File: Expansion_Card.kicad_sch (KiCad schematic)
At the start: 38 parts, among them J1 Conn_01x03_MountingPin, J2 Conn_01x03_MountingPin, P1 USB_C_Plug_USB2.0, SW1 SW_Push, SW2 SW_Push, U1 AP2112K-3.3, U2 RP2354A, Y1 ABM8-272-T3

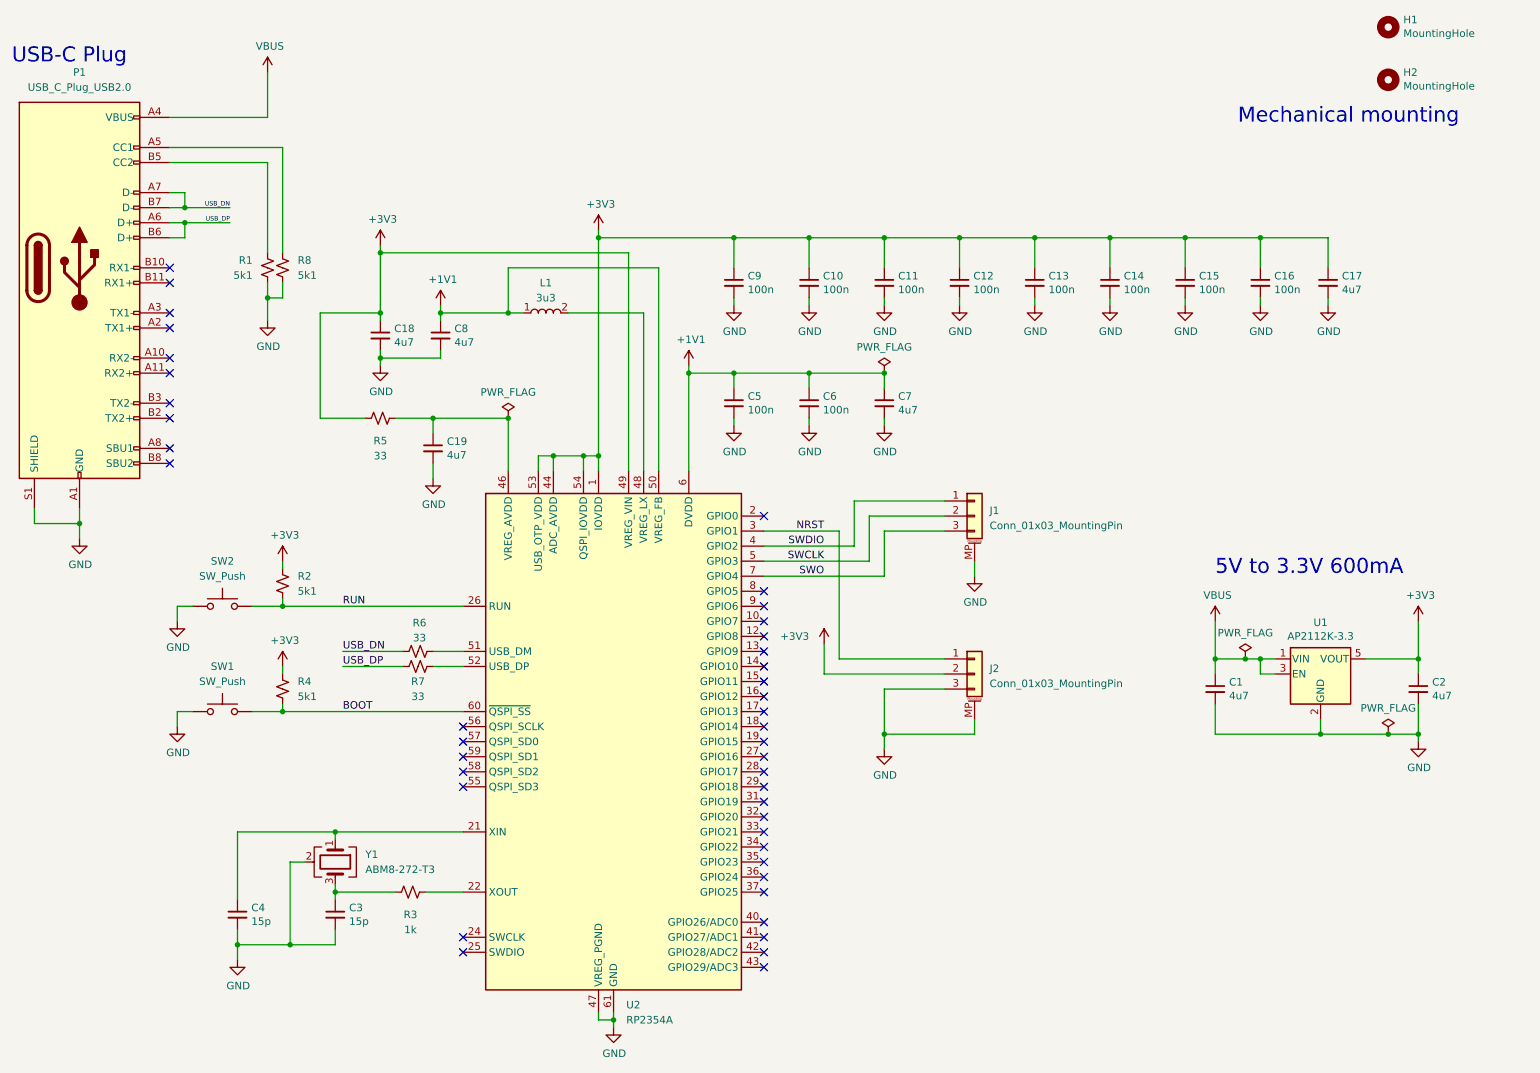
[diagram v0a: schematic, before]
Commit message: add fiducials/testpoints
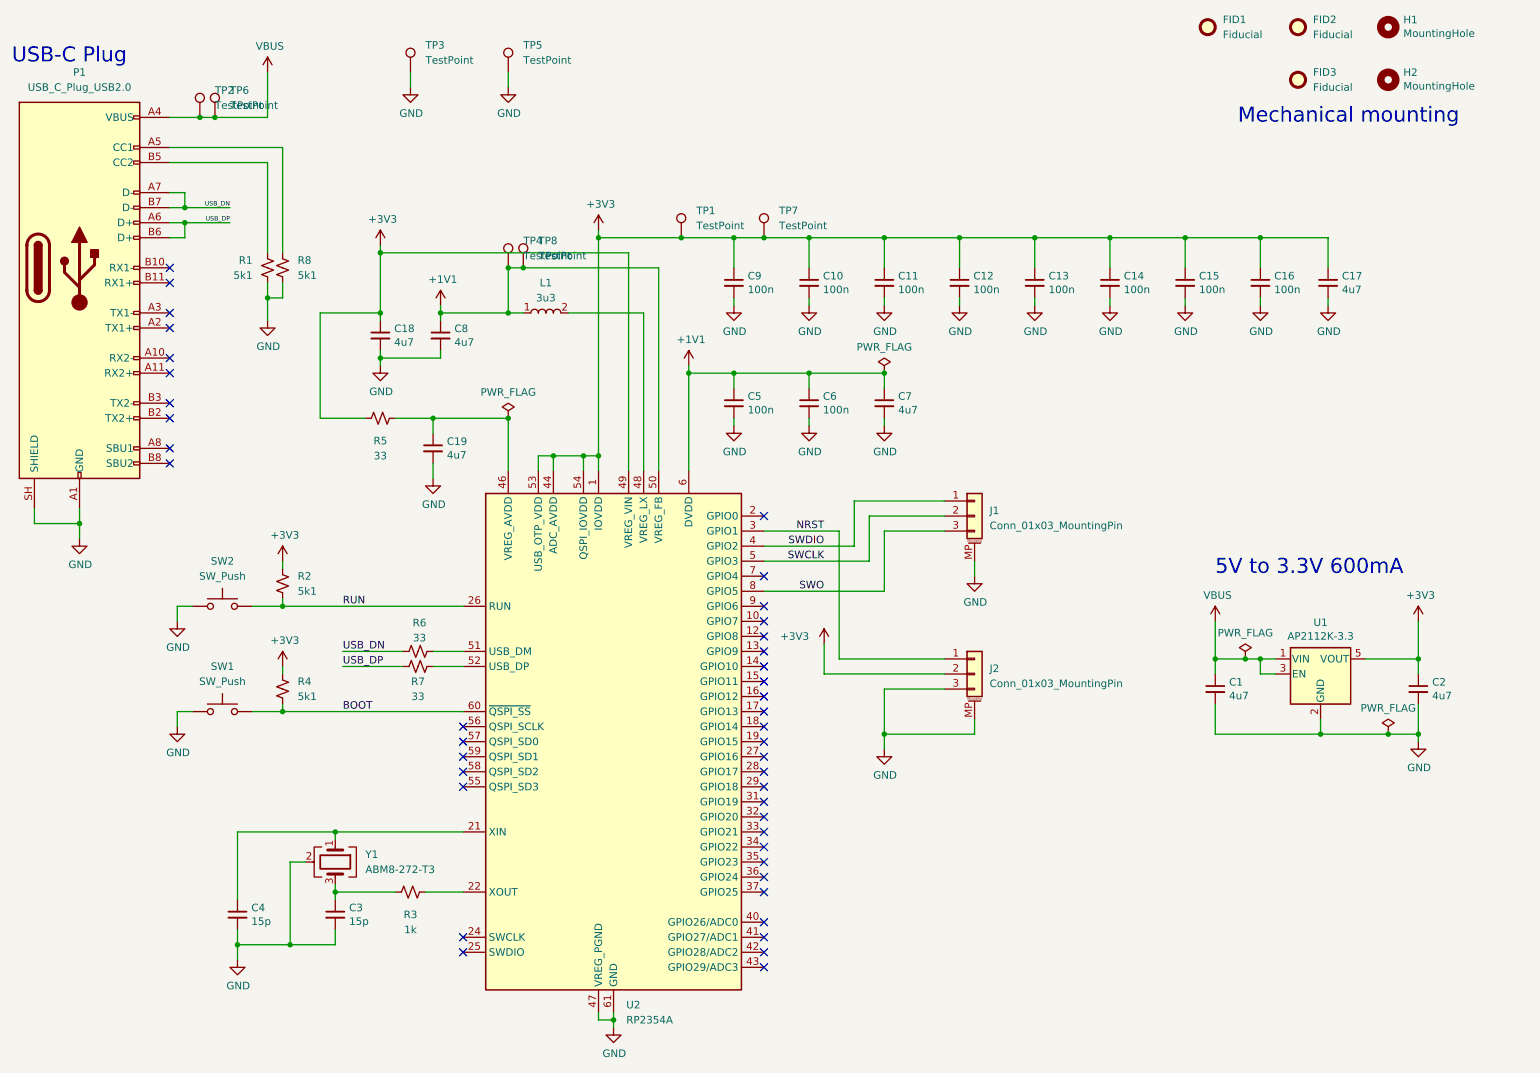
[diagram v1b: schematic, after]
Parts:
- added FID1, FID2, FID3: Fiducial, Fiducial:Fiducial_1mm_Mask2mm, symbol Mechanical:Fiducial
- added TP1, TP2, TP3, TP4, TP5, TP6, TP7, TP8: TestPoint, TestPoint:TestPoint_Pad_D1.5mm, symbol Connector:TestPoint
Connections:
- net +1V1: now also TP4.1, TP8.1
- net +3V3: now also TP1.1, TP7.1
- net GND: now also P1.SH (SHIELD), TP3.1, TP5.1; no longer P1.S1 (SHIELD)
- net SWO: now also U2.8 (GPIO5); no longer U2.7 (GPIO4)
- net VBUS: now also TP2.1, TP6.1
